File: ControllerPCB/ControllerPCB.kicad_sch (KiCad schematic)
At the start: 109 parts, among them J1 Conn_02x40_Row_Letter_First, SW1 SW_SPDT, U2 STM32F439ZITx, Y2 WE-XTAL_CFPX-218

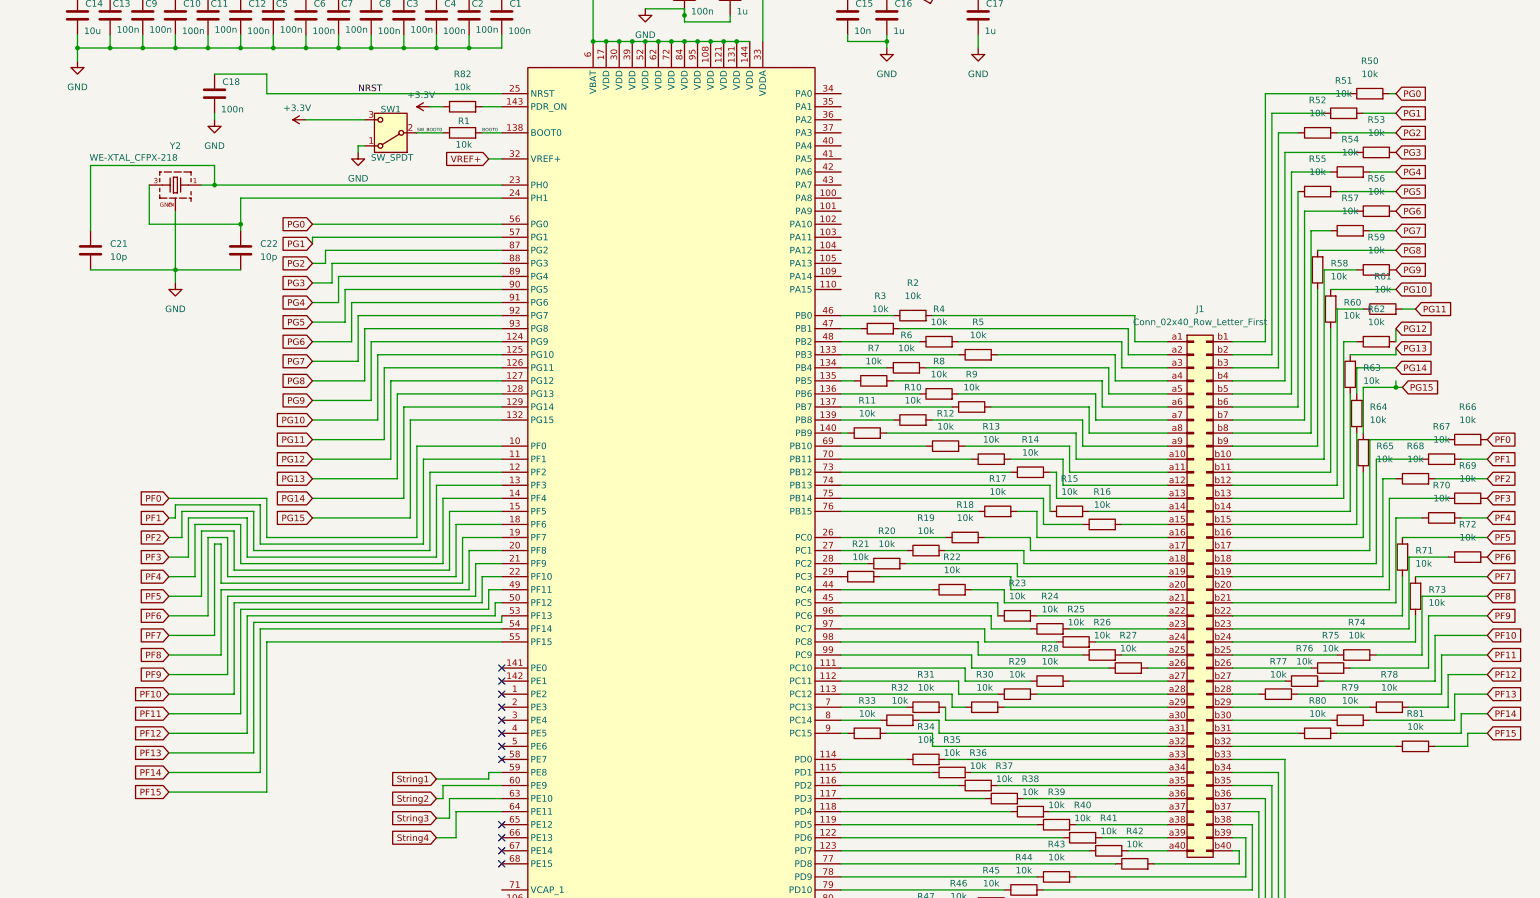
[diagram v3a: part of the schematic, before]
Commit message: rev 0.1
- power and amplitude sheets added
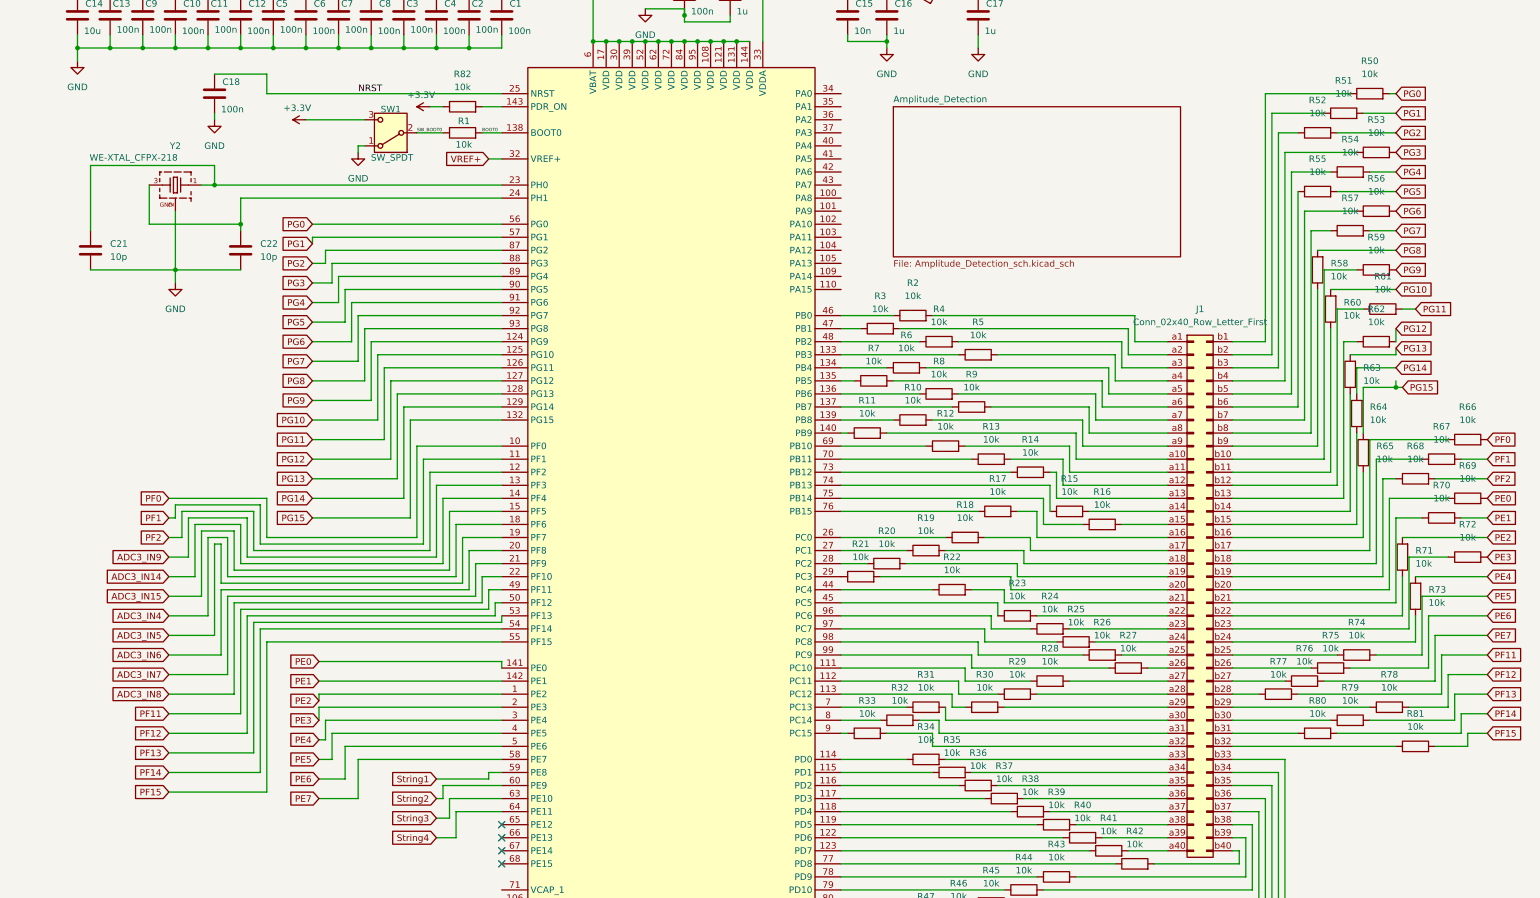
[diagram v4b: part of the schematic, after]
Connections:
- net PE2: now reaches U2.1 (PE2)
- net PE2: now also R71.2
- net PE0: now reaches U2.141 (PE0)
- net PE0: now also R69.2
- net PE1: now reaches U2.142 (PE1)
- net PE1: now also R70.2
- net PE3: now reaches U2.2 (PE3)
- net PE3: now also R72.2
- net PE4: now reaches U2.3 (PE4)
- net PE4: now also R73.2
- net PE5: now reaches U2.4 (PE5)
- net PE5: now also R74.2
- net PE6: now reaches U2.5 (PE6)
- net PE6: now also R75.2
- net PE7: now reaches U2.58 (PE7)
- net PE7: now also R76.2
- net PF10 renamed ADC3_IN8
- net ADC3_IN8: no longer R76.2
- net PF3 renamed ADC3_IN9
- net ADC3_IN9: no longer R69.2
- net PF4 renamed ADC3_IN14
- net ADC3_IN14: no longer R70.2
- net PF5 renamed ADC3_IN15
- net ADC3_IN15: no longer R71.2
- net PF6 renamed ADC3_IN4
- net ADC3_IN4: no longer R72.2
- net PF7 renamed ADC3_IN5
- net ADC3_IN5: no longer R73.2
- net PF8 renamed ADC3_IN6
- net ADC3_IN6: no longer R74.2
- net PF9 renamed ADC3_IN7
- net ADC3_IN7: no longer R75.2
- no-connect marks 12 -> 4
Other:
- added sheet Amplitude_Detection (Amplitude_Detection_sch.kicad_sch)
